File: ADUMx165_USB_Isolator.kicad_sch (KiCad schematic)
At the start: 61 parts, among them J1 XKB_U262-16XN-4BVC11, J2 HRO_TYPE-C-31-M-17, J3 XKB_U221-041N-4V33, J4 XKB_U221-041N-4V33, J5 XKB_U221-041N-4V33, J6 XKB_U221-041N-4V33, T1 DA2303-AL, U1 SN6505BDBV, U10 USBLC6-2P6, U2 USBLC6-2P6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

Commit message: Add GND Vias Update Workflow
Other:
- title: (none) -> ADUMx165 USB Isolator
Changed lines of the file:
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@@
 	(generator_version "8.0")
 	(paper "A4")
+	(title_block
+		(title "ADUMx165 USB Isolator")
+		(date "2024-11-15")
+		(rev "A")
+		(comment 1 "https://github.com/acha666/ADUMx165_USB_Isolator")
+	)
 	(junction
 		(at 58.42 109.22)

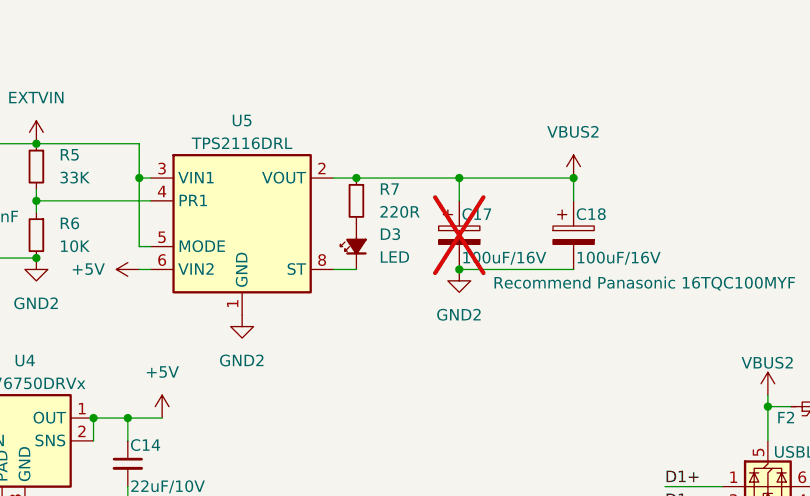
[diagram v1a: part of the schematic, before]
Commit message: Update readme.md Add Eng translation Add board image Change R7 value to 2K
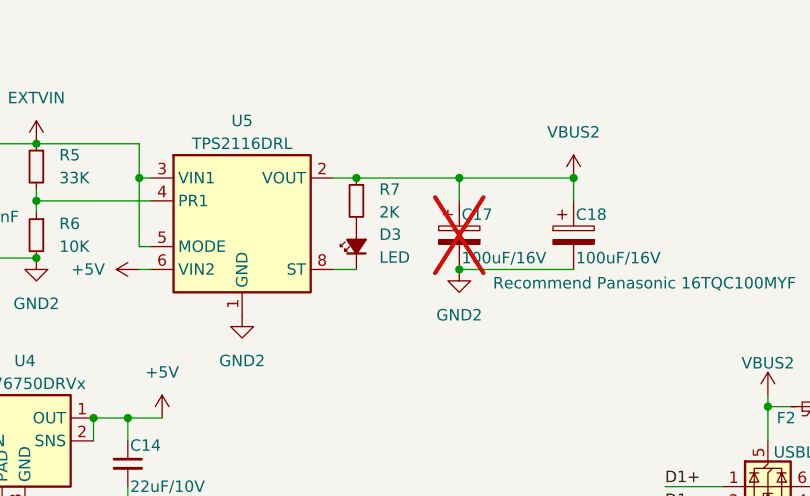
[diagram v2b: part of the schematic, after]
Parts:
- R7: value 220R -> 2K
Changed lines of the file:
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@@
 			)
 		)
-		(property "Value" "220R"
+		(property "Value" "2K"
 			(at 185.42 34.2899 0)
 			(effects

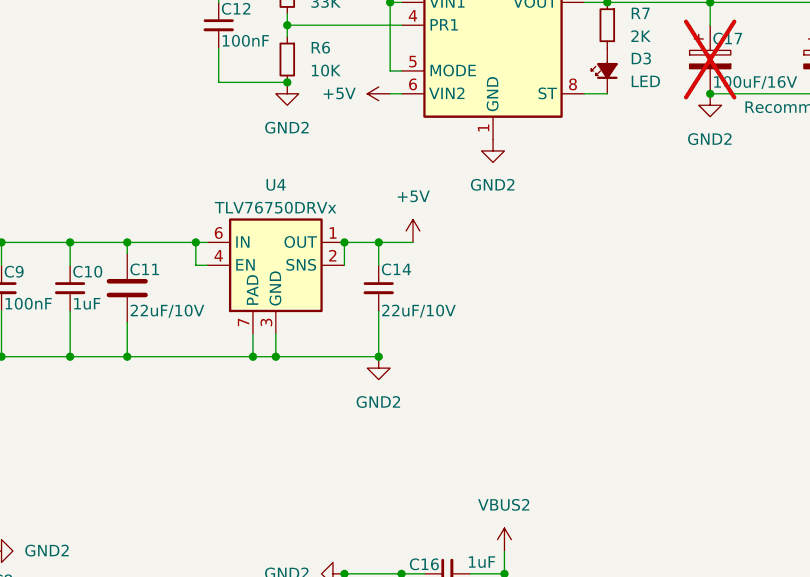
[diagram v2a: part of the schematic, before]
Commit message: Change TLV76750 to TLV76701
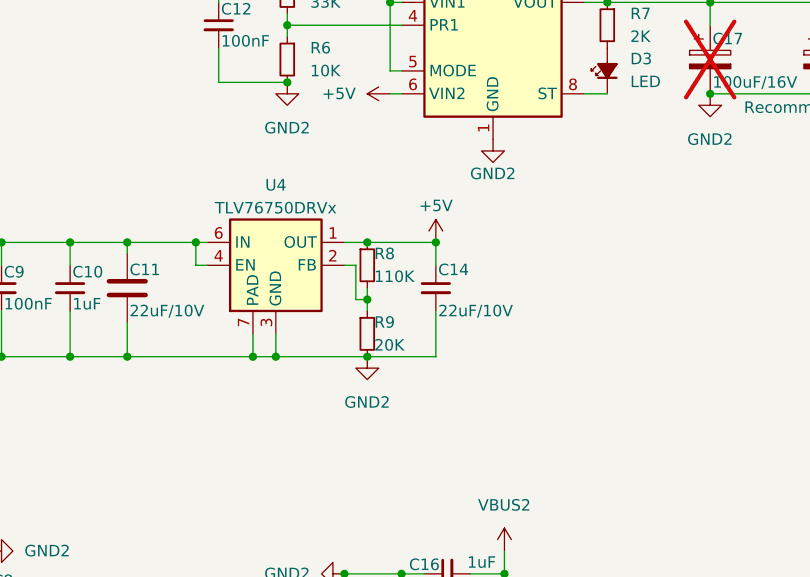
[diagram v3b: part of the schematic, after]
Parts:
- added R8: 110K, Resistor_SMD:R_0402_1005Metric, symbol Device:R_Small
- added R9: 20K, Resistor_SMD:R_0402_1005Metric, symbol Device:R_Small
- U4: symbol Regulator_Linear:TLV76750DRVx -> Regulator_Linear:TLV76701DRVx
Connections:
- net +5V: now also R8.1; no longer U4.2 (SNS)
- net GND2: now also R9.2
- new net: R8.2, R9.1, U4.2 (FB)
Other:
- moved on the sheet: C14
